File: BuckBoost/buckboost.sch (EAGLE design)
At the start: 13 parts

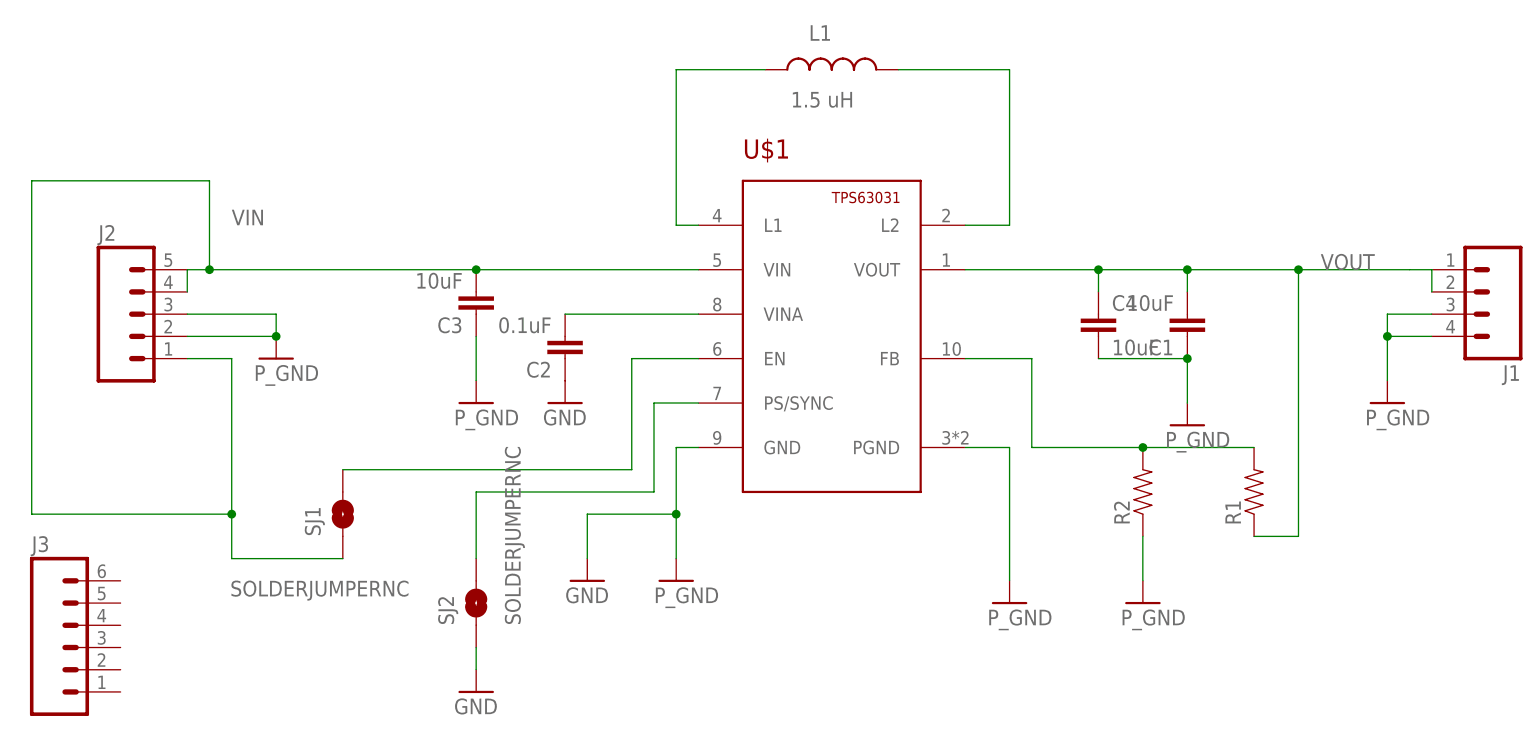
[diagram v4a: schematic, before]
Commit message: integrated 6 pin header
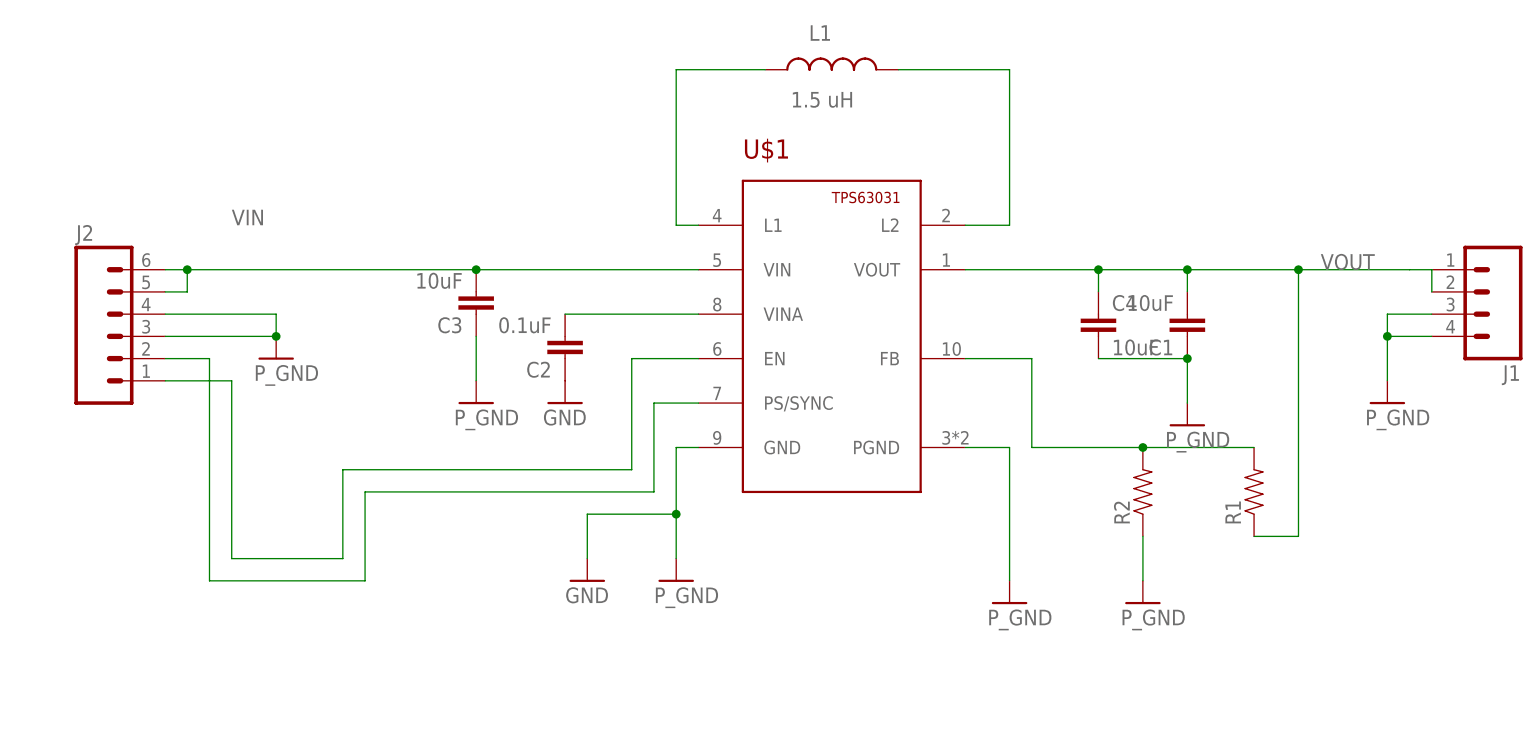
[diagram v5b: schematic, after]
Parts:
- removed J3: (no value), SparkFun-Connectors:M06SILK_FEMALE_PTH
- removed SJ1, SJ2: SOLDERJUMPERNC, SparkFun-Retired:SOLDERJUMPERNC
- J2: device SparkFun-Connectors:M05PTH -> SparkFun-Connectors:M06SILK_FEMALE_PTH
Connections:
- net GND: now also J2.4; no longer J2.2, SJ2.1
- net N$2: now also J2.1; no longer SJ1.2
- net N$4: now also J2.2; no longer SJ2.2
- net VIN: now also J2.6; no longer J2.1, J2.4, SJ1.1
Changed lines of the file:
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@@
 <part name="P_GND1" library="SparkFun-Aesthetics" deviceset="GND" device="" value="P_GND"/>
 <part name="J1" library="SparkFun-Connectors" deviceset="M04" device="PTH"/>
-<part name="J2" library="SparkFun-Connectors" deviceset="M05" device="PTH"/>
-<part name="SJ1" library="SparkFun-Retired" deviceset="SOLDERJUMPER" device="NC"/>
 <part name="P_GND2" library="SparkFun-Aesthetics" deviceset="GND" device="" value="P_GND"/>
-<part name="SJ2" library="SparkFun-Retired" deviceset="SOLDERJUMPER" device="NC"/>
-<part name="GND5" library="SparkFun-Aesthetics" deviceset="GND" device=""/>
 <part name="P_GND3" library="SparkFun-Aesthetics" deviceset="GND" device="" value="P_GND"/>
-<part name="J3" library="SparkFun-Connectors" deviceset="M06" device="SILK_FEMALE_PTH"/>
+<part name="J2" library="SparkFun-Connectors" deviceset="M06" device="SILK_FEMALE_PTH"/>
 </parts>
 <sheets>
@@
 <instance part="P_GND1" gate="1" x="200.66" y="-55.88"/>
 <instance part="J1" gate="G$1" x="238.76" y="-20.32" rot="R180"/>
-<instance part="J2" gate="G$1" x="83.82" y="-22.86"/>
-<instance part="SJ1" gate="1" x="109.22" y="-45.72" smashed="yes" rot="R90">
-<attribute name="NAME" x="106.68" y="-48.26" size="1.778" layer="95" rot="R90"/>
-<attribute name="VALUE" x="116.84" y="-53.34" size="1.778" layer="96" rot="R180"/>
-</instance>
 <instance part="P_GND2" gate="1" x="101.6" y="-27.94"/>
-<instance part="SJ2" gate="1" x="124.46" y="-55.88" rot="R90"/>
-<instance part="GND5" gate="1" x="124.46" y="-66.04"/>
 <instance part="P_GND3" gate="1" x="228.6" y="-33.02"/>
-<instance part="J3" gate="G$1" x="78.74" y="-60.96"/>
+<instance part="J2" gate="G$1" x="83.82" y="-25.4"/>
 </instances>
 <busses>
@@
 <wire x1="149.86" y1="-17.78" x2="124.46" y2="-17.78" width="0.1524" layer="91"/>
 <junction x="124.46" y="-17.78"/>
-<wire x1="124.46" y1="-17.78" x2="93.98" y2="-17.78" width="0.1524" layer="91"/>
+<wire x1="124.46" y1="-17.78" x2="91.44" y2="-17.78" width="0.1524" layer="91"/>
 <label x="96.52" y="-12.7" size="1.778" layer="95"/>
+<wire x1="91.44" y1="-17.78" x2="91.44" y2="-20.32" width="0.1524" layer="91"/>
+<pinref part="J2" gate="G$1" pin="6"/>
+<wire x1="88.9" y1="-17.78" x2="91.44" y2="-17.78" width="0.1524" layer="91"/>
+<junction x="91.44" y="-17.78"/>
 <pinref part="J2" gate="G$1" pin="5"/>
-<pinref part="J2" gate="G$1" pin="4"/>
-<wire x1="93.98" y1="-17.78" x2="91.44" y2="-17.78" width="0.1524" layer="91"/>
-<wire x1="91.44" y1="-17.78" x2="91.44" y2="-20.32" width="0.1524" layer="91"/>
-<wire x1="93.98" y1="-17.78" x2="93.98" y2="-7.62" width="0.1524" layer="91"/>
-<junction x="93.98" y="-17.78"/>
-<wire x1="93.98" y1="-7.62" x2="73.66" y2="-7.62" width="0.1524" layer="91"/>
-<wire x1="73.66" y1="-7.62" x2="73.66" y2="-45.72" width="0.1524" layer="91"/>
-<pinref part="J2" gate="G$1" pin="1"/>
-<wire x1="91.44" y1="-27.94" x2="96.52" y2="-27.94" width="0.1524" layer="91"/>
-<wire x1="96.52" y1="-27.94" x2="96.52" y2="-45.72" width="0.1524" layer="91"/>
-<pinref part="SJ1" gate="1" pin="1"/>
-<wire x1="96.52" y1="-45.72" x2="96.52" y2="-50.8" width="0.1524" layer="91"/>
-<wire x1="96.52" y1="-50.8" x2="109.22" y2="-50.8" width="0.1524" layer="91"/>
-<wire x1="73.66" y1="-45.72" x2="96.52" y2="-45.72" width="0.1524" layer="91"/>
-<junction x="96.52" y="-45.72"/>
+<wire x1="91.44" y1="-20.32" x2="88.9" y2="-20.32" width="0.1524" layer="91"/>
 </segment>
 </net>
@@
 </segment>
 <segment>
-<pinref part="J2" gate="G$1" pin="3"/>
-<wire x1="91.44" y1="-22.86" x2="101.6" y2="-22.86" width="0.1524" layer="91"/>
+<wire x1="88.9" y1="-22.86" x2="101.6" y2="-22.86" width="0.1524" layer="91"/>
 <pinref part="P_GND2" gate="1" pin="GND"/>
 <wire x1="101.6" y1="-22.86" x2="101.6" y2="-25.4" width="0.1524" layer="91"/>
-<pinref part="J2" gate="G$1" pin="2"/>
-<wire x1="91.44" y1="-25.4" x2="101.6" y2="-25.4" width="0.1524" layer="91"/>
+<wire x1="88.9" y1="-25.4" x2="101.6" y2="-25.4" width="0.1524" layer="91"/>
 <junction x="101.6" y="-25.4"/>
-</segment>
-<segment>
-<pinref part="SJ2" gate="1" pin="1"/>
-<pinref part="GND5" gate="1" pin="GND"/>
-<wire x1="124.46" y1="-60.96" x2="124.46" y2="-63.5" width="0.1524" layer="91"/>
+<pinref part="J2" gate="G$1" pin="4"/>
+<pinref part="J2" gate="G$1" pin="3"/>
 </segment>
 <segment>
@@
 <pinref part="U$1" gate="G$1" pin="EN"/>
 <wire x1="149.86" y1="-27.94" x2="142.24" y2="-27.94" width="0.1524" layer="91"/>
-<pinref part="SJ1" gate="1" pin="2"/>
 <wire x1="109.22" y1="-40.64" x2="142.24" y2="-40.64" width="0.1524" layer="91"/>
 <wire x1="142.24" y1="-40.64" x2="142.24" y2="-27.94" width="0.1524" layer="91"/>
+<wire x1="96.52" y1="-50.8" x2="109.22" y2="-50.8" width="0.1524" layer="91"/>
+<wire x1="109.22" y1="-40.64" x2="109.22" y2="-50.8" width="0.1524" layer="91"/>
+<wire x1="96.52" y1="-50.8" x2="96.52" y2="-30.48" width="0.1524" layer="91"/>
+<pinref part="J2" gate="G$1" pin="1"/>
+<wire x1="96.52" y1="-30.48" x2="88.9" y2="-30.48" width="0.1524" layer="91"/>
 </segment>
 </net>
@@
 <wire x1="149.86" y1="-33.02" x2="144.78" y2="-33.02" width="0.1524" layer="91"/>
 <wire x1="144.78" y1="-33.02" x2="144.78" y2="-43.18" width="0.1524" layer="91"/>
-<pinref part="SJ2" gate="1" pin="2"/>
-<wire x1="144.78" y1="-43.18" x2="124.46" y2="-43.18" width="0.1524" layer="91"/>
-<wire x1="124.46" y1="-43.18" x2="124.46" y2="-50.8" width="0.1524" layer="91"/>
-</segment>
-</net>
+<wire x1="144.78" y1="-43.18" x2="111.76" y2="-43.18" width="0.1524" layer="91"/>
+<wire x1="93.98" y1="-53.34" x2="111.76" y2="-53.34" width="0.1524" layer="91"/>
+<wire x1="111.76" y1="-53.34" x2="111.76" y2="-43.18" width="0.1524" layer="91"/>
+<wire x1="93.98" y1="-53.34" x2="93.98" y2="-27.94" width="0.1524" layer="91"/>
+<pinref part="J2" gate="G$1" pin="2"/>
+<wire x1="93.98" y1="-27.94" x2="88.9" y2="-27.94" width="0.1524" layer="91"/>
+</segment>
+</net>

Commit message: Added Jumpers
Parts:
- added SJ1, SJ2: SOLDERJUMPERNC, SparkFun-Retired:SOLDERJUMPERNC
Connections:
- removed net N$2: J2.1, U$1.EN
- new net N$5: J2.1, SJ1.1, U$1.EN
- net N$3: now also SJ1.2, SJ2.1
- net N$4: now also SJ2.2
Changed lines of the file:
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@@
 <part name="P_GND3" library="SparkFun-Aesthetics" deviceset="GND" device="" value="P_GND"/>
 <part name="J2" library="SparkFun-Connectors" deviceset="M06" device="SILK_FEMALE_PTH"/>
+<part name="SJ1" library="SparkFun-Retired" deviceset="SOLDERJUMPER" device="NC"/>
+<part name="SJ2" library="SparkFun-Retired" deviceset="SOLDERJUMPER" device="NC"/>
 </parts>
 <sheets>
@@
 <instance part="P_GND3" gate="1" x="228.6" y="-33.02"/>
 <instance part="J2" gate="G$1" x="83.82" y="-25.4"/>
+<instance part="SJ1" gate="1" x="93.98" y="-63.5" rot="R180"/>
+<instance part="SJ2" gate="1" x="119.38" y="-63.5" rot="R180"/>
 </instances>
 <busses>
@@
 <pinref part="C2" gate="G$1" pin="2"/>
 <wire x1="149.86" y1="-22.86" x2="134.62" y2="-22.86" width="0.1524" layer="91"/>
+<wire x1="134.62" y1="-22.86" x2="129.54" y2="-22.86" width="0.1524" layer="91"/>
+<wire x1="129.54" y1="-22.86" x2="129.54" y2="-60.96" width="0.1524" layer="91"/>
+<pinref part="SJ2" gate="1" pin="1"/>
+<wire x1="129.54" y1="-60.96" x2="124.46" y2="-60.96" width="0.1524" layer="91"/>
+<wire x1="124.46" y1="-60.96" x2="124.46" y2="-63.5" width="0.1524" layer="91"/>
+<pinref part="SJ1" gate="1" pin="2"/>
+<wire x1="88.9" y1="-63.5" x2="76.2" y2="-63.5" width="0.1524" layer="91"/>
+<wire x1="76.2" y1="-63.5" x2="76.2" y2="-7.62" width="0.1524" layer="91"/>
+<wire x1="76.2" y1="-7.62" x2="129.54" y2="-7.62" width="0.1524" layer="91"/>
+<wire x1="129.54" y1="-7.62" x2="129.54" y2="-22.86" width="0.1524" layer="91"/>
+<junction x="129.54" y="-22.86"/>
 </segment>
 </net>
@@
 </segment>
 </net>
-<net name="N$2" class="0">
-<segment>
+<net name="N$4" class="0">
+<segment>
+<pinref part="U$1" gate="G$1" pin="PS/SYNC"/>
+<wire x1="149.86" y1="-33.02" x2="144.78" y2="-33.02" width="0.1524" layer="91"/>
+<wire x1="144.78" y1="-33.02" x2="144.78" y2="-43.18" width="0.1524" layer="91"/>
+<wire x1="144.78" y1="-43.18" x2="111.76" y2="-43.18" width="0.1524" layer="91"/>
+<wire x1="93.98" y1="-53.34" x2="111.76" y2="-53.34" width="0.1524" layer="91"/>
+<wire x1="111.76" y1="-53.34" x2="111.76" y2="-43.18" width="0.1524" layer="91"/>
+<wire x1="93.98" y1="-53.34" x2="93.98" y2="-27.94" width="0.1524" layer="91"/>
+<pinref part="J2" gate="G$1" pin="2"/>
+<wire x1="93.98" y1="-27.94" x2="88.9" y2="-27.94" width="0.1524" layer="91"/>
+<pinref part="SJ2" gate="1" pin="2"/>
+<wire x1="114.3" y1="-63.5" x2="111.76" y2="-63.5" width="0.1524" layer="91"/>
+<wire x1="111.76" y1="-63.5" x2="111.76" y2="-53.34" width="0.1524" layer="91"/>
+<junction x="111.76" y="-53.34"/>
+</segment>
+</net>
+<net name="N$5" class="0">
+<segment>
+<pinref part="SJ1" gate="1" pin="1"/>
+<wire x1="99.06" y1="-63.5" x2="109.22" y2="-63.5" width="0.1524" layer="91"/>
 <pinref part="U$1" gate="G$1" pin="EN"/>
 <wire x1="149.86" y1="-27.94" x2="142.24" y2="-27.94" width="0.1524" layer="91"/>
@@
 <pinref part="J2" gate="G$1" pin="1"/>
 <wire x1="96.52" y1="-30.48" x2="88.9" y2="-30.48" width="0.1524" layer="91"/>
-</segment>
-</net>
-<net name="N$4" class="0">
-<segment>
-<pinref part="U$1" gate="G$1" pin="PS/SYNC"/>
-<wire x1="149.86" y1="-33.02" x2="144.78" y2="-33.02" width="0.1524" layer="91"/>
-<wire x1="144.78" y1="-33.02" x2="144.78" y2="-43.18" width="0.1524" layer="91"/>
-<wire x1="144.78" y1="-43.18" x2="111.76" y2="-43.18" width="0.1524" layer="91"/>
-<wire x1="93.98" y1="-53.34" x2="111.76" y2="-53.34" width="0.1524" layer="91"/>
-<wire x1="111.76" y1="-53.34" x2="111.76" y2="-43.18" width="0.1524" layer="91"/>
-<wire x1="93.98" y1="-53.34" x2="93.98" y2="-27.94" width="0.1524" layer="91"/>
-<pinref part="J2" gate="G$1" pin="2"/>
-<wire x1="93.98" y1="-27.94" x2="88.9" y2="-27.94" width="0.1524" layer="91"/>
-</segment>
-</net>
+<wire x1="109.22" y1="-63.5" x2="109.22" y2="-50.8" width="0.1524" layer="91"/>
+<junction x="109.22" y="-50.8"/>
+</segment>
+</net>

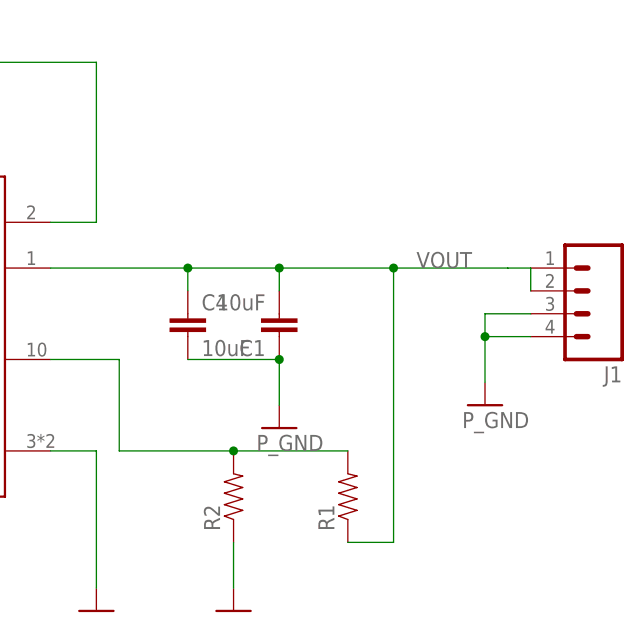
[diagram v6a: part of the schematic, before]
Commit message: Added vout_vfb jumper
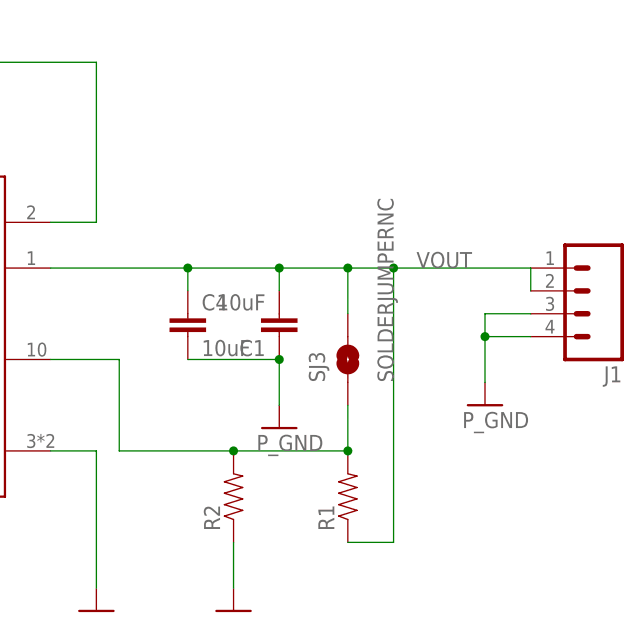
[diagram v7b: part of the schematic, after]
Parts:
- added SJ3: SOLDERJUMPERNC, SparkFun-Retired:SOLDERJUMPERNC
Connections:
- net N$1: now also SJ3.1
- net VOUT: now also SJ3.2
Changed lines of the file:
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@@
 <part name="SJ1" library="SparkFun-Retired" deviceset="SOLDERJUMPER" device="NC"/>
 <part name="SJ2" library="SparkFun-Retired" deviceset="SOLDERJUMPER" device="NC"/>
+<part name="SJ3" library="SparkFun-Retired" deviceset="SOLDERJUMPER" device="NC"/>
 </parts>
 <sheets>
@@
 <instance part="SJ1" gate="1" x="93.98" y="-63.5" rot="R180"/>
 <instance part="SJ2" gate="1" x="119.38" y="-63.5" rot="R180"/>
+<instance part="SJ3" gate="1" x="213.36" y="-27.94" rot="R90"/>
 </instances>
 <busses>
@@
 <wire x1="180.34" y1="-17.78" x2="195.58" y2="-17.78" width="0.1524" layer="91"/>
 <wire x1="195.58" y1="-17.78" x2="205.74" y2="-17.78" width="0.1524" layer="91"/>
-<wire x1="205.74" y1="-17.78" x2="218.44" y2="-17.78" width="0.1524" layer="91"/>
+<wire x1="205.74" y1="-17.78" x2="213.36" y2="-17.78" width="0.1524" layer="91"/>
+<wire x1="213.36" y1="-17.78" x2="218.44" y2="-17.78" width="0.1524" layer="91"/>
 <wire x1="205.74" y1="-20.32" x2="205.74" y2="-17.78" width="0.1524" layer="91"/>
 <junction x="205.74" y="-17.78"/>
@@
 <junction x="218.44" y="-17.78"/>
 <pinref part="J1" gate="G$1" pin="1"/>
-<wire x1="218.44" y1="-17.78" x2="231.14" y2="-17.78" width="0.1524" layer="91"/>
+<wire x1="218.44" y1="-17.78" x2="233.68" y2="-17.78" width="0.1524" layer="91"/>
 <pinref part="J1" gate="G$1" pin="2"/>
-<wire x1="231.14" y1="-17.78" x2="233.68" y2="-17.78" width="0.1524" layer="91"/>
 <wire x1="233.68" y1="-17.78" x2="233.68" y2="-20.32" width="0.1524" layer="91"/>
+<pinref part="SJ3" gate="1" pin="2"/>
+<wire x1="213.36" y1="-17.78" x2="213.36" y2="-22.86" width="0.1524" layer="91"/>
+<junction x="213.36" y="-17.78"/>
 </segment>
 </net>
@@
 <pinref part="U$1" gate="G$1" pin="FB"/>
 <wire x1="187.96" y1="-27.94" x2="180.34" y2="-27.94" width="0.1524" layer="91"/>
+<pinref part="SJ3" gate="1" pin="1"/>
+<wire x1="213.36" y1="-33.02" x2="213.36" y2="-38.1" width="0.1524" layer="91"/>
+<junction x="213.36" y="-38.1"/>
 </segment>
 </net>
